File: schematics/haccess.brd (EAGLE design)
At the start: 76 x 76 mm, 43 parts, among them IC1 ATMEGA32U2-TQFP, IC2 REG1117, Q2 BSS123, SW1 SPST_TACT-EVQQ2

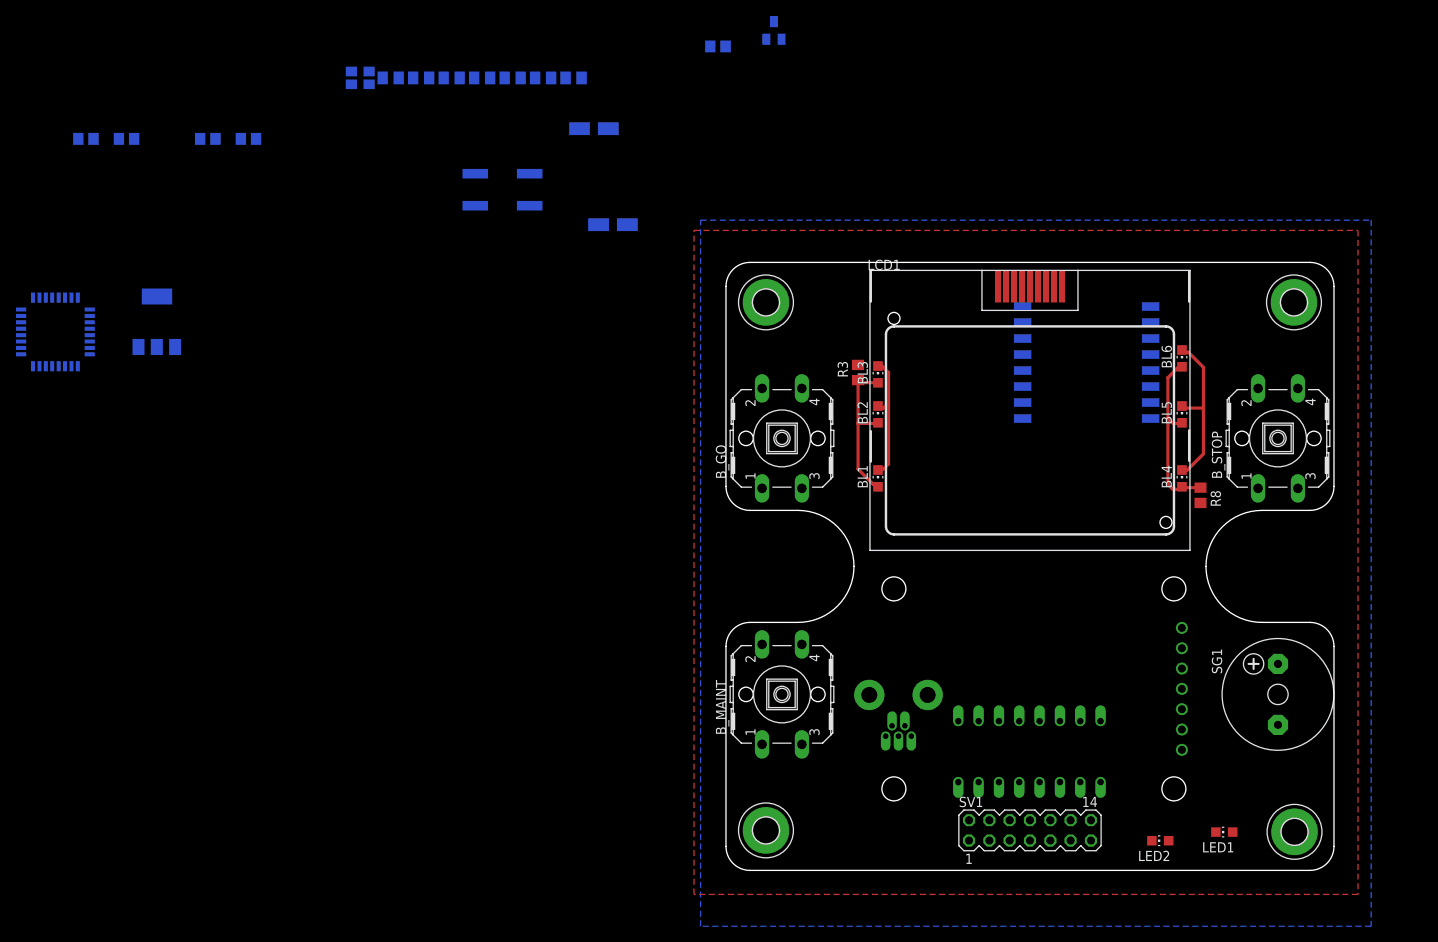
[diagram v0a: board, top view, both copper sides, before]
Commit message: Imported DXF of outline, got all important tuff into place, began routing
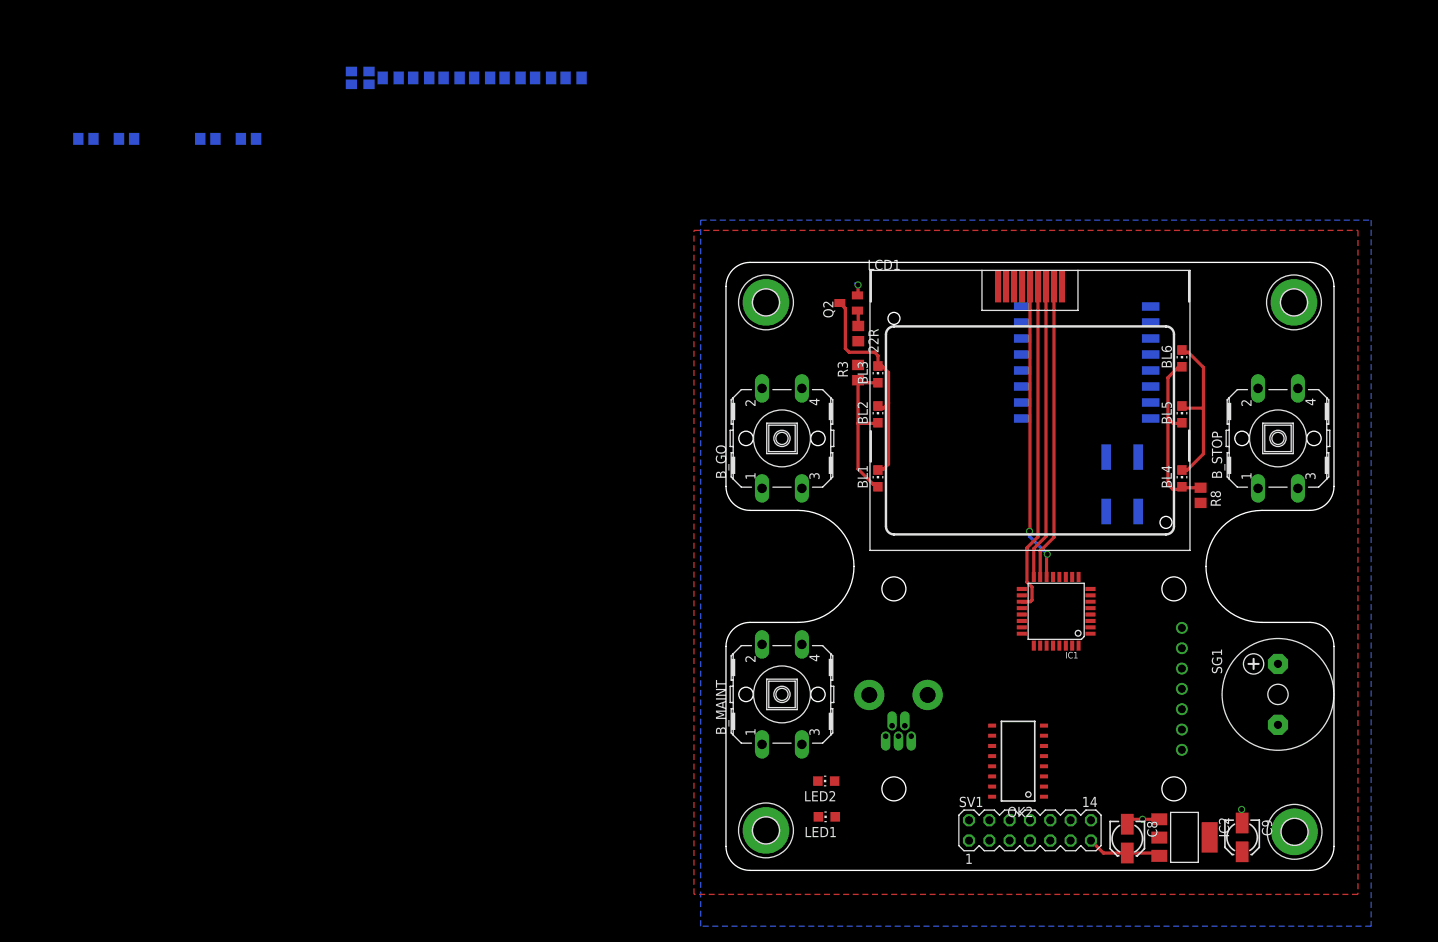
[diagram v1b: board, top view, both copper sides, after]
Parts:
- removed OK1: PC847, optocoupler:DIL16
- added OK2: TLP283-4, optocoupler:MINI-FLAT-16
- moved IC2 143.7 mm to (57.3, 4.13), flipped to the top, turned to 270 degrees
- moved IC1 129.9 mm to (41.3, 32.4), flipped to the top, turned to 180 degrees
- moved C8 111.0 mm to (50.2, 3.97), flipped to the top, turned to 270 degrees
- moved C9 109.8 mm to (64.5, 4.13), flipped to the top, turned to 270 degrees
- moved SW1 85.8 mm to (49.5, 48.3), turned to 90 degrees
- moved LED1 49.7 mm to (12.6, 6.70)
- moved LED2 42.4 mm to (12.5, 11.2)
- moved 22R 40.0 mm to (16.5, 67.1), flipped to the top, turned to 270 degrees
- moved Q2 35.3 mm to (15.3, 70.9), flipped to the top, turned to 90 degrees
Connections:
- net GND: now also OK2.14, OK2.16; no longer OK1.10, OK1.12
- net IN1_A: now also OK2.1; no longer OK1.5
- net IN1_C: now also OK2.2; no longer OK1.6
- net IN2_A: now also OK2.4; no longer OK1.8
- net IN2_C: now also OK2.3; no longer OK1.7
- net N$10: now also OK2.6; no longer OK1.2
- net N$11: now also OK2.8; no longer OK1.4
- net N$13: now also OK2.13; no longer OK1.9
- net N$15: now also OK2.15; no longer OK1.11
- net N$16: now also OK2.7, R5.2; no longer OK1.1, R4.2
- net N$20: now also OK2.5, R4.2; no longer OK1.3, R5.2
- net OUT1_A: now also OK2.10; no longer OK1.14
- net OUT1_C: now also OK2.9; no longer OK1.13
- net OUT2_A: now also OK2.12; no longer OK1.16
- net OUT2_C: now also OK2.11; no longer OK1.15
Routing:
- net LCD_DC: track 0.00 -> 41.4 mm
- net !LCD_CS: track 0.00 -> 37.3 mm, vias 0 -> 2
- net SCK: track 0.00 -> 37.0 mm
- net MOSI: track 0.00 -> 37.0 mm
- net N$18: track 37.1 -> 48.8 mm
- net V+: track 0.00 -> 9.33 mm
- net GND: track 0.00 -> 8.04 mm, vias 0 -> 3
- net N$22: track 0.00 -> 1.97 mm

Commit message: Routed board
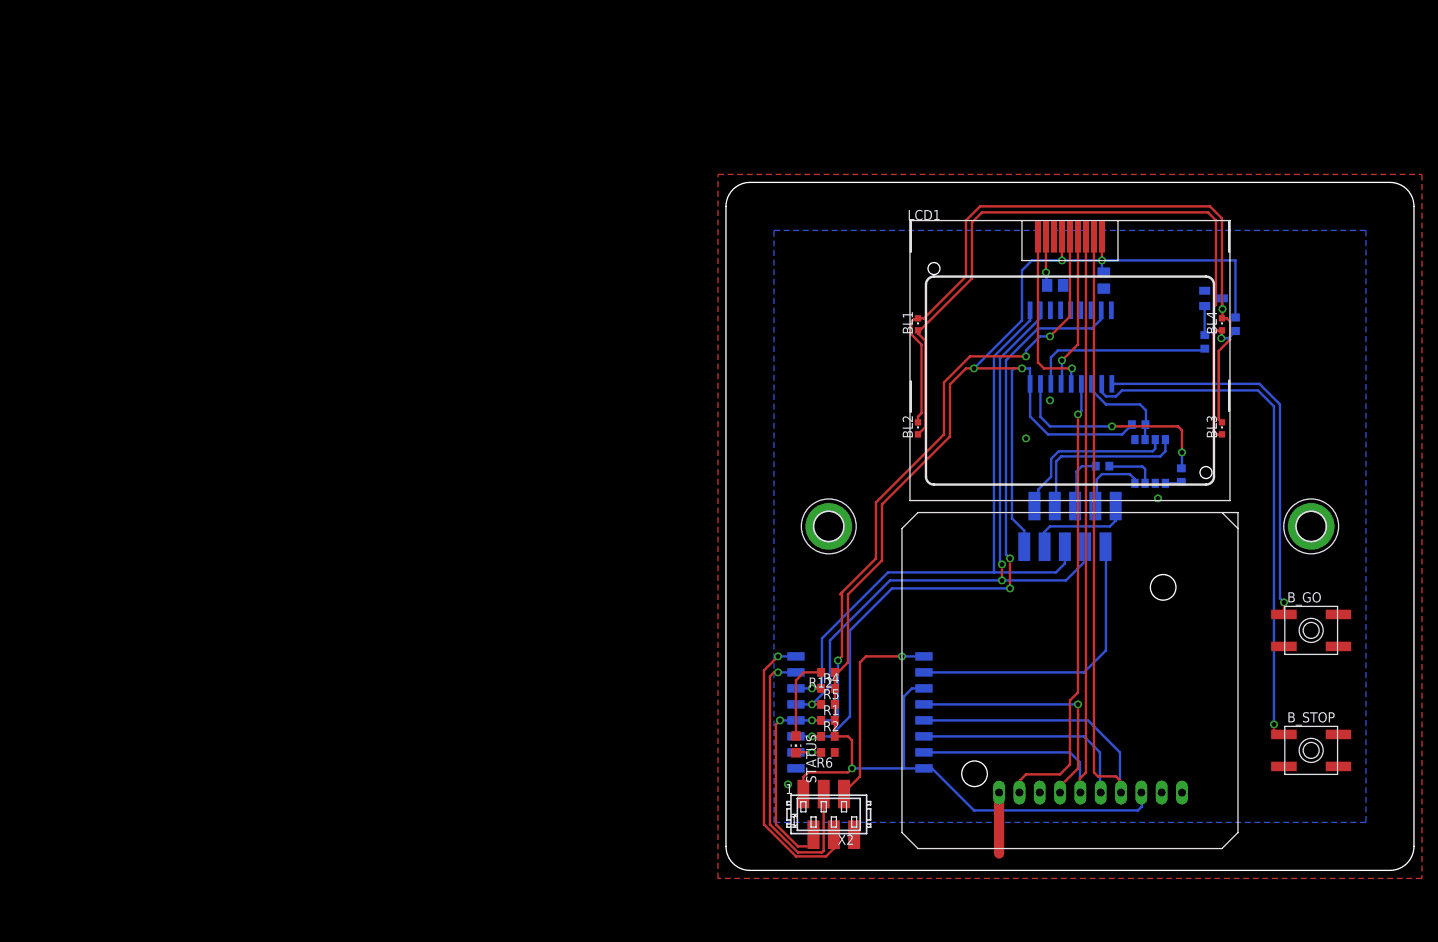
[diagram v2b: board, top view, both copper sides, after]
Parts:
- removed 22R, R8: (no value), rcl:R0805
- removed BL5, BL6, LED1, LED2: (no value), led:CHIP-LED0805
- removed B_MAINT: (no value), switch-omron:B3F-40XX
- removed C3, C4, C5, C6, C7: (no value), rcl:C0805K
- removed C8, C9: (no value), rcl:153CLV-0405
- removed CN1: (no value), adafruit:USB-MINIB-THM-MOLEX
- removed H3, H4: MOUNT-PAD-ROUND3.2, holes:3,2-PAD
- removed IC2: REG1117, burr-brown:SOT223
- removed OK2: TLP283-4, optocoupler:MINI-FLAT-16
- removed Q1: (no value), adafruit:NX3225
- removed SG1: F/CM12P, buzzer:F/CM12P
- removed SV1: (no value), con-lstb:MA07-2
- removed SW1: SPST_TACT-EVQQ2, adafruit:EVQ-Q2
- added IO: MICROMATCH-10-SMD, tyco:MICROMATCH-10-SMD
- added R10, R12, R9: 220R, rcl:R0603
- added R11, R6: 4K7, rcl:R0603
- added R7: 22R, rcl:R0603
- added STATUS: (no value), led:CHIP-LED0805
- added U$3: OPTOISOLATOR-2SOIC8, SparkFun-DiscreteSemi:SO08-2
- added X2: MICROMATCH-6-SMD, tyco:MICROMATCH-6-SMD
- BL1, BL2, BL3, BL4: device led:CHIP-LED0805 -> led:CHIPLED_0603
- B_GO, B_STOP: value (none) -> SPST_TACT-EVQQ2; device switch-omron:B3F-40XX -> adafruit:EVQ-Q2
- C1, C2: value (none) -> 100nF
- H1, H2: value MOUNT-PAD-ROUND3.2 -> MOUNT-PAD-ROUND3.6; device holes:3,2-PAD -> holes:3,6-PAD
- IC1: value ATMEGA32U2-TQFP -> MCP2300X/SO; device adafruit:TQFP32-08 -> adafruit:SO18W
- R1, R2, R4, R5: value (none) -> 4K7; device rcl:R0805 -> rcl:R0603
- R3: value (none) -> 22R; device rcl:R0805 -> rcl:R0603
- U$1: value FM1701 -> PN532SMALLMODULE; device FM1701:FM1701 -> PN532:SMALL-MODULE
- moved R5 116.6 mm to (12.8, 20.8), flipped to the top
- moved R4 111.4 mm to (12.8, 22.8), flipped to the top
- moved R2 107.6 mm to (12.8, 16.8), flipped to the top
- moved R1 102.6 mm to (12.8, 18.8), flipped to the top
- moved C2 74.5 mm to (47.2, 73.7), turned to 270 degrees
- moved H2 73.7 mm to (73.2, 43.0)
- moved B_GO 70.4 mm to (73.2, 30.0), turned to 0 degrees
- moved C1 65.5 mm to (41.1, 73.1), turned to 180 degrees
- moved H1 64.5 mm to (12.8, 43.0)
- moved U$2 52.1 mm to (16.8, 26.8)
- moved R3 47.6 mm to (63.7, 68.3), flipped to the bottom
- moved Q2 45.6 mm to (60.9, 71.5), flipped to the bottom
- moved BL3 43.5 mm to (62.0, 55.2)
- moved B_STOP 39.2 mm to (73.2, 15.0), turned to 0 degrees
- moved IC1 33.0 mm to (42.5, 65.4), flipped to the bottom
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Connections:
- removed net !ESP_RST: U$2.RESET
- removed net !LCD_CS: IC1.14, LCD1.5
- removed net !LCD_RST: IC1.18, LCD1.9
- removed net !RFID_CS: IC1.21, U$1.!SS
- removed net !RFID_RST: IC1.20, U$1.RST
- removed net D+: CN1.D+, IC1.29
- removed net D-: CN1.D-, IC1.30
- removed net IN1_A: OK2.1, SV1.10
- removed net IN1_C: OK2.2, SV1.9
- removed net IN2_A: OK2.4, SV1.8
- removed net IN2_C: OK2.3, SV1.7
- removed net LCD_DC: IC1.19, LCD1.4
- removed net N$10: IC1.23, OK2.6
- removed net N$11: OK2.8
- removed net N$12: C5.2, IC1.27
- removed net N$13: IC1.22, OK2.13
- removed net N$14: B_MAINT.1, IC1.13
- removed net N$15: IC1.26, OK2.15
- removed net N$16: OK2.7, R5.2
- removed net N$17: LED2.A, R2.1
- removed net N$20: OK2.5, R4.2
- removed net N$21: 22R.2, IC1.10
- removed net N$23: BL4.A, BL5.A, BL6.A, R8.1
- removed net N$24: IC1.5, SG1.+
- removed net N$5: B_GO.1, IC1.6
- removed net N$6: B_STOP.1, IC1.7
- removed net N$7: IC1.24, SW1.B
- removed net OUT1_A: OK2.10, SV1.6
- removed net OUT1_C: OK2.9, SV1.5
- removed net OUT2_A: OK2.12, SV1.4
- removed net OUT2_C: OK2.11, SV1.3
- removed net RX: IC1.8, U$2.TXD
- removed net TX: IC1.9, U$2.RXD
- removed net V+: C7.2, C8.+, IC2.3, SV1.13, SV1.14
- removed net VUSB: CN1.VBUS, IC1.31
- new net !IRQ: IC1.8, R2.1, U$2.GPIO2
- new net !OUT_RESET_PERIPH: IC1.14, LCD1.9
- new net !RST: IC1.6
- new net ADC: IO.9, U$2.ADC
- new net CS0: LCD1.5, R1.1, U$2.GPIO0, X2.2
- new net CS1: U$1.!SS, U$2.GPIO16
- new net IN_532_IRQ: IC1.13, U$1.IRQ
- new net IN_G: B_STOP.B, IC1.11
- new net IN_OPTO: IC1.12, R11.2, U$3.6
- new net IN_OPTO_A: IO.6, R10.2
- new net IN_OPTO_C: IO.8, U$3.4
- new net IN_R: B_GO.B, IC1.10
- new net OUT_LCD_BL: IC1.16, R7.2
- new net OUT_LCD_DC: IC1.15, LCD1.4
- new net OUT_OPTO: IC1.17, R9.2
- new net OUT_STATUS_LED: R6.2, STATUS.C, U$2.GPIO15
- new net PROG_RESET: U$2.RESET, X2.5
- new net PROG_RX: U$2.RXD, X2.3
- new net PROG_TX: U$2.TXD, X2.4
- new net SCL: IC1.1, IO.5, R4.1, U$2.GPIO4
- new net SDA: IC1.2, IO.7, R5.1, U$2.GPIO5
- net +3V3: now also IC1.18, IO.1, R11.1, R12.1, R4.2, R5.2, U$1.3V3, X2.1; no longer C6.2, C9.+, IC1.32, IC1.4, IC2.2, R4.1, R5.1, R8.2, SV1.11, SV1.12, U$1.VCC, U$2.GPIO0, U$2.GPIO2
- net GND: now also B_GO.A, B_STOP.A, H1.B3,6, H2.B3,6, IC1.4, IC1.5, IC1.9, IO.10, IO.3, R6.1, U$3.2, U$3.5, X2.6; no longer B_GO.3, B_MAINT.3, B_STOP.3, C3.1, C4.1, C5.1, C6.1, C7.1, C8.-, C9.-, CN1.GND, H1.B3,2, H2.B3,2, H3.B3,2, H4.B3,2, IC1.28, IC2.1, OK2.14, OK2.16, Q1.2, Q1.4, SG1.-, SV1.1, SV1.2, SW1.A, U$2.GPIO15
- net MISO: now also U$2.GPIO12; no longer IC1.17
- net MOSI: now also U$2.GPIO13; no longer IC1.16
- net N$18: no longer BL5.C, BL6.C
- net N$19: now also BL4.A
- net N$2: now also R12.2, STATUS.A; no longer IC1.11, LED1.C
- net N$22: now also R7.1; no longer 22R.1
- net N$3: now also R9.1, U$3.1; no longer IC1.12, LED2.C
- net N$4: now also R10.1, U$3.3; no longer LED1.A, R1.1
- net N$8: now also IO.4, U$3.8; no longer C4.2, IC1.2, Q1.3
- net N$9: now also IO.2, U$3.7; no longer C3.2, IC1.1, Q1.1
- net SCK: now also U$2.GPIO14; no longer IC1.15
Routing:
- net +3V3: track 0.00 -> 228.7 mm, vias 0 -> 5
- net CS0: track 0.00 -> 106.0 mm, vias 0 -> 5
- net SDA: track 0.00 -> 86.0 mm, vias 0 -> 3
- net !IRQ: track 0.00 -> 85.7 mm, vias 0 -> 3
- net SCL: track 0.00 -> 81.2 mm, vias 0 -> 1
- net N$19: track 19.7 -> 93.7 mm, vias 0 -> 1
- net SCK: track 37.0 -> 103.4 mm
- net IN_G: track 0.00 -> 66.2 mm, vias 0 -> 1
- net IN_532_IRQ: track 0.00 -> 56.8 mm, vias 0 -> 1
- net MOSI: track 37.0 -> 93.6 mm
- net IN_R: track 0.00 -> 48.5 mm, vias 0 -> 1
- net N$18: track 48.8 -> 91.4 mm, vias 0 -> 1
- net LCD_DC: track 41.4 -> 0.00 mm
- net !LCD_CS: track 37.3 -> 0.00 mm, vias 2 -> 0
- net PROG_RX: track 0.00 -> 37.3 mm, vias 0 -> 1
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- added copper zone on layer 1, net GND
- removed copper zone on layer 1, net +3V3
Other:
- board size 76 x 76 mm -> 86 x 86 mm

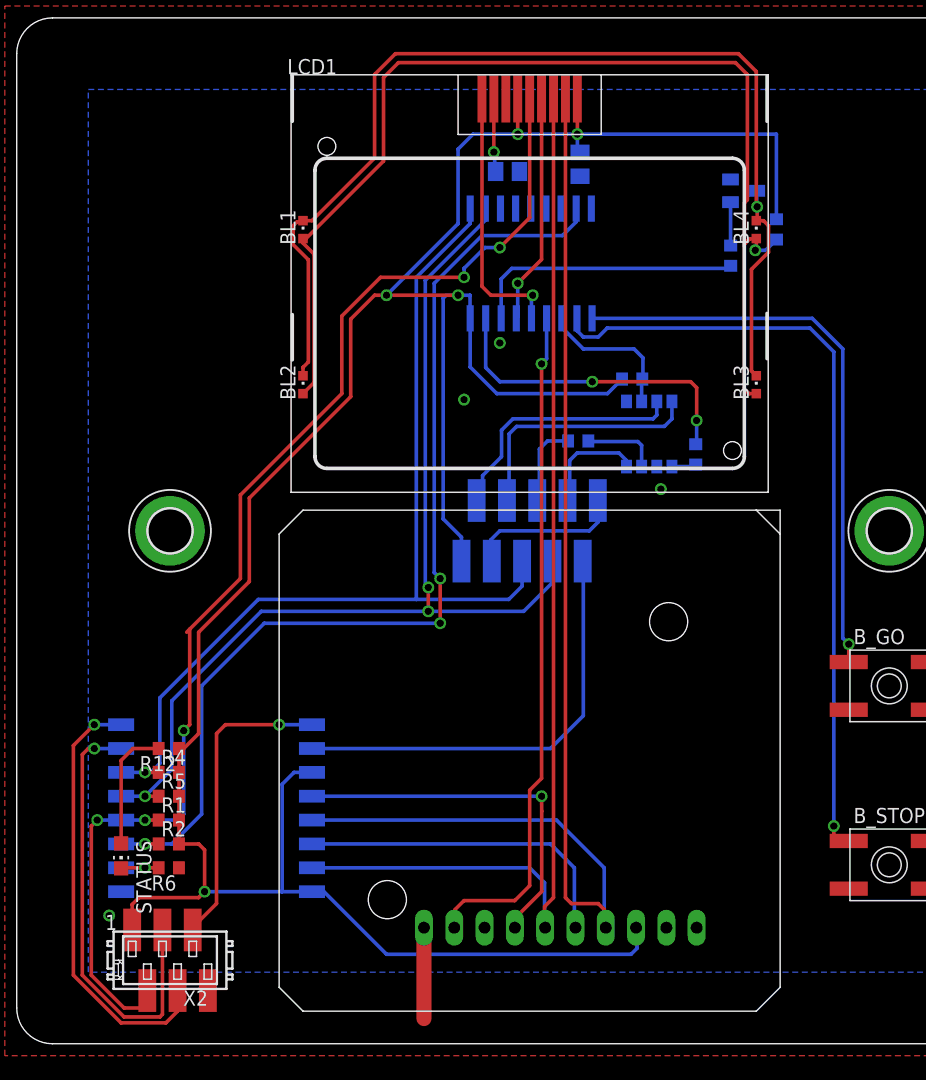
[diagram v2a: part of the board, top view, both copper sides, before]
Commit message: Ran DRC, added holes for mounting LCD
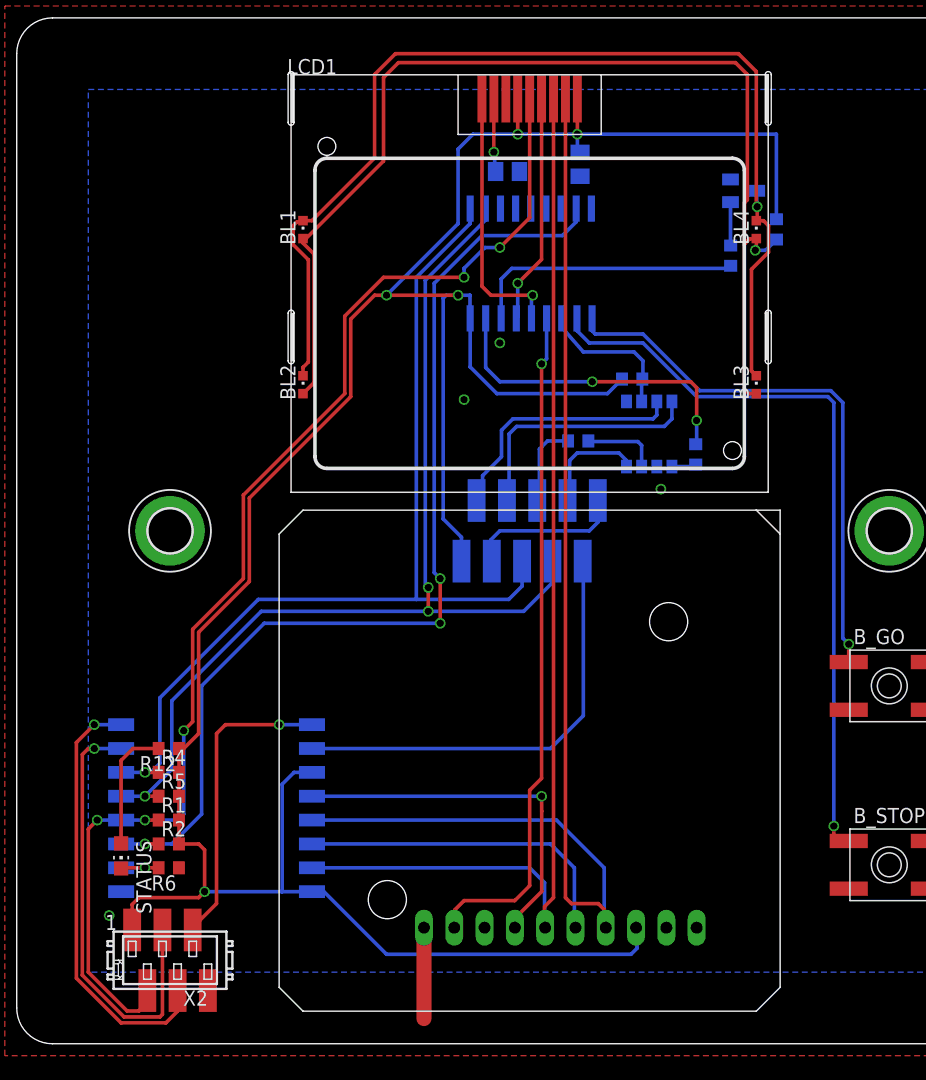
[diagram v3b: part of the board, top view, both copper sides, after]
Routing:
- net IN_G: track 66.2 -> 63.1 mm
- net IN_R: track 48.5 -> 46.5 mm
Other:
- outline, holes or cut-outs redrawn
